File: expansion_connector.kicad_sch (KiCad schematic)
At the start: 18 parts, among them J18 ASP-218650-01_mounting_holes, J19 Plug_Samtec_UMPT-06-06.5-G-V-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

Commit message: [#83396] WIP: Route PCIe on expansion connector, change Expansion connector pinout to ease out routing PCIe
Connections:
- net DP1.AUX+: now also J18.B08; no longer J18.Y18
- net DP1.AUX-: now also J18.B09; no longer J18.Y19
- net DP1.TX0+: now also J18.B12; no longer J18.Y22
- net DP1.TX0-: now also J18.B13; no longer J18.Y23
- net DP1.TX1+: now also J18.B16; no longer J18.Y26
- net DP1.TX1-: now also J18.B17; no longer J18.Y27
- net DP1.TX2+: now also J18.B20; no longer J18.Y30
- net DP1.TX2-: now also J18.B21; no longer J18.Y31
- net DP1.TX3+: now also J18.B24; no longer J18.Y34
- net DP1.TX3-: now also J18.B25; no longer J18.Y35
- net PCIe_{C2x1}.CLK+: now also J18.Y38; no longer J18.B20
- net PCIe_{C2x1}.CLK-: now also J18.Y39; no longer J18.B21
- net PCIe_{C2x1}.RX0+: now also J18.Y35; no longer J18.B13
- net PCIe_{C2x1}.RX0-: now also J18.Y34; no longer J18.B12
- net PCIe_{C2x1}.~{CLKREQ}: now also J18.Z13; no longer J18.B17
- net PCIe_{C2x1}.~{RST}: now also J18.Z12; no longer J18.B16
- net PCIe_{C3x2}.CLK+: now also J18.Y27; no longer J18.Z21
- net PCIe_{C3x2}.CLK-: now also J18.Y26; no longer J18.Z20
- net PCIe_{C3x2}.RX0+: now also J18.Y19; no longer J18.Z17
- net PCIe_{C3x2}.RX0-: now also J18.Y18; no longer J18.Z16
- net PCIe_{C3x2}.RX1+: now also J18.Y23; no longer J18.Z13
- net PCIe_{C3x2}.RX1-: now also J18.Y22; no longer J18.Z12
- net PET0_C2_N: now also J18.Y31; no longer J18.B09
- net PET0_C2_P: now also J18.Y30; no longer J18.B08
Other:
- note removed: "----CSI----"
- note removed: "----PCIE----"
- note removed: "----RGMII----"
- note removed: "65 L K ... B A 64 . : 2 1"
- note removed: "AGX"
- note removed: "FMC"
- note removed: "M 40 39 38 ... 4 3 2 1 L K . : B A Z Y"
- note removed: "Perypherials"
- note removed: "We can change FMC pinout according to how hard it woud be to route it"
- note removed: "Z1 Y6 ... Y1"
- moved on the sheet: C213, C214

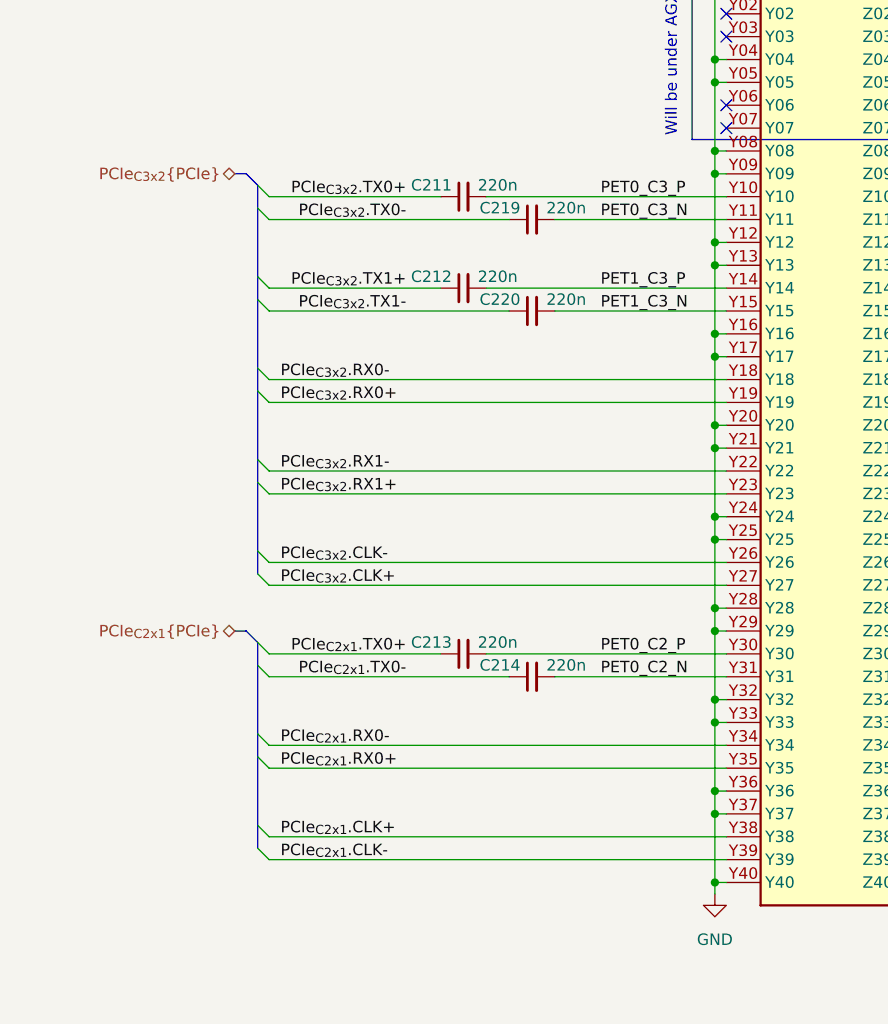
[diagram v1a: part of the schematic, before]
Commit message: [#83396] Route PCIe on expansion connector
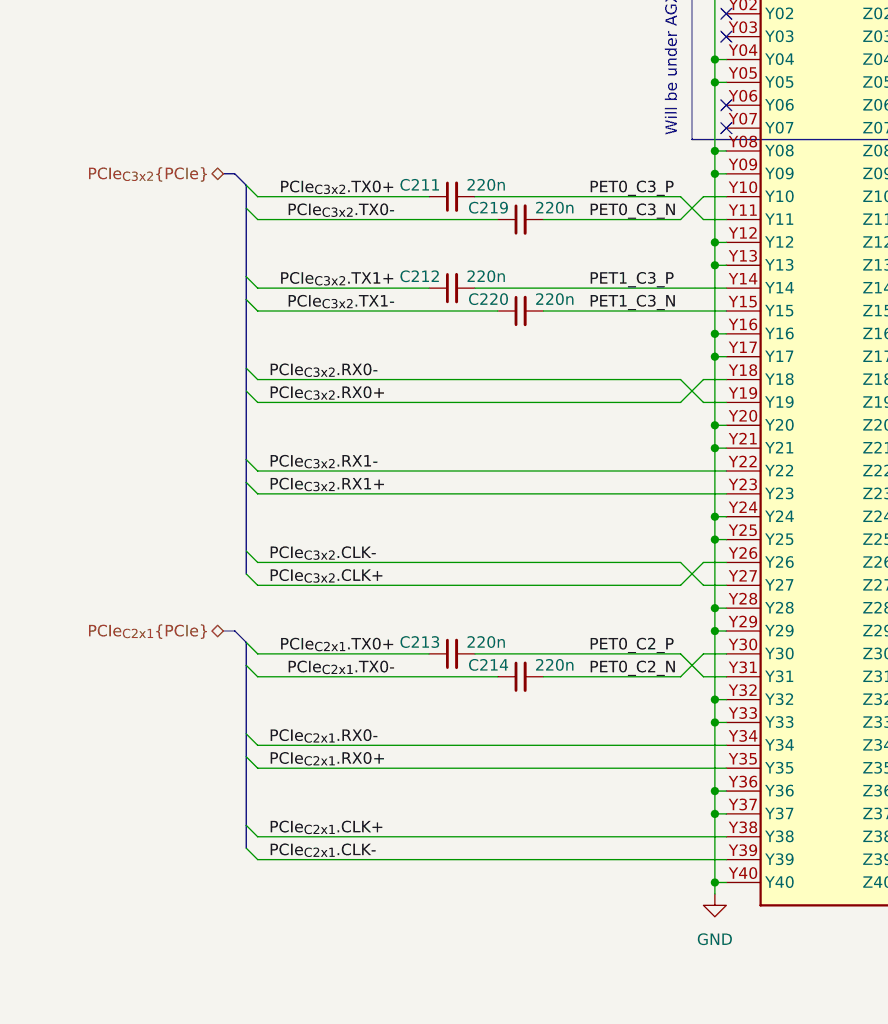
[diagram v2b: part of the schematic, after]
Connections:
- net PCIe_{C3x2}.CLK+: now also J18.Y26; no longer J18.Y27
- net PCIe_{C3x2}.CLK-: now also J18.Y27; no longer J18.Y26
- net PCIe_{C3x2}.RX0+: now also J18.Y18; no longer J18.Y19
- net PCIe_{C3x2}.RX0-: now also J18.Y19; no longer J18.Y18
- net PET0_C2_N: now also J18.Y30; no longer J18.Y31
- net PET0_C2_P: now also J18.Y31; no longer J18.Y30
- net PET0_C3_N: now also J18.Y10; no longer J18.Y11
- net PET0_C3_P: now also J18.Y11; no longer J18.Y10
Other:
- moved on the sheet: C211, C212, C213, C214, C219, C220

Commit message: [#83396] WIP: Route out DP
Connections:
- net DP1.AUX+: now also J18.A22; no longer J18.B08
- net DP1.AUX-: now also J18.A23; no longer J18.B09
- net DP1.TX0+: now also J18.A26; no longer J18.B12
- net DP1.TX0-: now also J18.A27; no longer J18.B13
- net DP1.TX1+: now also J18.A30; no longer J18.B16
- net DP1.TX1-: now also J18.A31; no longer J18.B17
- net DP1.TX2+: now also J18.A34; no longer J18.B20
- net DP1.TX2-: now also J18.A35; no longer J18.B21
- net DP1.TX3+: now also J18.A38; no longer J18.B24
- net DP1.TX3-: now also J18.A39; no longer J18.B25
- net DP3.AUX+: now also J18.B08; no longer J18.A22
- net DP3.AUX-: now also J18.B09; no longer J18.A23
- net DP3.TX0+: now also J18.B12; no longer J18.A26
- net DP3.TX0-: now also J18.B13; no longer J18.A27
- net DP3.TX1+: now also J18.B16; no longer J18.A30
- net DP3.TX1-: now also J18.B17; no longer J18.A31
- net DP3.TX2+: now also J18.B20; no longer J18.A34
- net DP3.TX2-: now also J18.B21; no longer J18.A35
- net DP3.TX3+: now also J18.B24; no longer J18.A38
- net DP3.TX3-: now also J18.B25; no longer J18.A39
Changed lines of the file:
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@@
 	)
 	(label "DP3.TX3-"
-		(at 74.93 260.35 0)
-		(effects
-			(font
-				(size 1.27 1.27)
-			)
-			(justify left bottom)
+		(at 125.73 224.79 180)
+		(effects
+			(font
+				(size 1.27 1.27)
+			)
+			(justify right bottom)
 		)
 	)
@@
 	)
 	(label "DP3.TX2+"
-		(at 74.93 247.65 0)
-		(effects
-			(font
-				(size 1.27 1.27)
-			)
-			(justify left bottom)
+		(at 125.73 212.09 180)
+		(effects
+			(font
+				(size 1.27 1.27)
+			)
+			(justify right bottom)
 		)
 	)
@@
 	)
 	(label "DP3.TX0+"
-		(at 74.93 227.33 0)
-		(effects
-			(font
-				(size 1.27 1.27)
-			)
-			(justify left bottom)
+		(at 125.73 191.77 180)
+		(effects
+			(font
+				(size 1.27 1.27)
+			)
+			(justify right bottom)
 		)
 	)
@@
 	)
 	(label "DP1.TX1+"
-		(at 125.73 201.93 180)
-		(effects
-			(font
-				(size 1.27 1.27)
-			)
-			(justify right bottom)
+		(at 74.93 237.49 0)
+		(effects
+			(font
+				(size 1.27 1.27)
+			)
+			(justify left bottom)
 		)
 	)
@@
 	)
 	(label "DP1.TX1-"
-		(at 125.73 204.47 180)
-		(effects
-			(font
-				(size 1.27 1.27)
-			)
-			(justify right bottom)
+		(at 74.93 240.03 0)
+		(effects
+			(font
+				(size 1.27 1.27)
+			)
+			(justify left bottom)
 		)
 	)
@@
 	)
 	(label "DP1.TX2+"
-		(at 125.73 212.09 180)
-		(effects
-			(font
-				(size 1.27 1.27)
-			)
-			(justify right bottom)
+		(at 74.93 247.65 0)
+		(effects
+			(font
+				(size 1.27 1.27)
+			)
+			(justify left bottom)
 		)
 	)
@@
 	)
 	(label "DP1.TX2-"
-		(at 125.73 214.63 180)
-		(effects
-			(font
-				(size 1.27 1.27)
-			)
-			(justify right bottom)
+		(at 74.93 250.19 0)
+		(effects
+			(font
+				(size 1.27 1.27)
+			)
+			(justify left bottom)
 		)
 	)
@@
 	)
 	(label "DP3.AUX+"
-		(at 74.93 217.17 0)
-		(effects
-			(font
-				(size 1.27 1.27)
-			)
-			(justify left bottom)
+		(at 125.73 181.61 180)
+		(effects
+			(font
+				(size 1.27 1.27)
+			)
+			(justify right bottom)
 		)
 	)
@@
 	)
 	(label "DP3.AUX-"
-		(at 74.93 219.71 0)
-		(effects
-			(font
-				(size 1.27 1.27)
-			)
-			(justify left bottom)
+		(at 125.73 184.15 180)
+		(effects
+			(font
+				(size 1.27 1.27)
+			)
+			(justify right bottom)
 		)
 	)
@@
 	)
 	(label "DP3.TX0-"
-		(at 74.93 229.87 0)
-		(effects
-			(font
-				(size 1.27 1.27)
-			)
-			(justify left bottom)
+		(at 125.73 194.31 180)
+		(effects
+			(font
+				(size 1.27 1.27)
+			)
+			(justify right bottom)
 		)
 	)
@@
 	)
 	(label "DP1.TX3-"
-		(at 125.73 224.79 180)
-		(effects
-			(font
-				(size 1.27 1.27)
-			)
-			(justify right bottom)
+		(at 74.93 260.35 0)
+		(effects
+			(font
+				(size 1.27 1.27)
+			)
+			(justify left bottom)
 		)
 	)
@@
 	)
 	(label "DP1.TX0-"
-		(at 125.73 194.31 180)
-		(effects
-			(font
-				(size 1.27 1.27)
-			)
-			(justify right bottom)
+		(at 74.93 229.87 0)
+		(effects
+			(font
+				(size 1.27 1.27)
+			)
+			(justify left bottom)
 		)
 	)
@@
 	)
 	(label "DP3.TX1-"
-		(at 74.93 240.03 0)
-		(effects
-			(font
-				(size 1.27 1.27)
-			)
-			(justify left bottom)
+		(at 125.73 204.47 180)
+		(effects
+			(font
+				(size 1.27 1.27)
+			)
+			(justify right bottom)
 		)
 	)
@@
 	)
 	(label "DP1.AUX+"
-		(at 125.73 181.61 180)
-		(effects
-			(font
-				(size 1.27 1.27)
-			)
-			(justify right bottom)
+		(at 74.93 217.17 0)
+		(effects
+			(font
+				(size 1.27 1.27)
+			)
+			(justify left bottom)
 		)
 	)
@@
 	)
 	(label "DP1.AUX-"
-		(at 125.73 184.15 180)
-		(effects
-			(font
-				(size 1.27 1.27)
-			)
-			(justify right bottom)
+		(at 74.93 219.71 0)
+		(effects
+			(font
+				(size 1.27 1.27)
+			)
+			(justify left bottom)
 		)
 	)
@@
 	)
 	(label "DP1.TX3+"
-		(at 125.73 222.25 180)
-		(effects
-			(font
-				(size 1.27 1.27)
-			)
-			(justify right bottom)
+		(at 74.93 257.81 0)
+		(effects
+			(font
+				(size 1.27 1.27)
+			)
+			(justify left bottom)
 		)
 	)
@@
 	)
 	(label "DP1.TX0+"
-		(at 125.73 191.77 180)
-		(effects
-			(font
-				(size 1.27 1.27)
-			)
-			(justify right bottom)
+		(at 74.93 227.33 0)
+		(effects
+			(font
+				(size 1.27 1.27)
+			)
+			(justify left bottom)
 		)
 	)
@@
 	)
 	(label "DP3.TX2-"
-		(at 74.93 250.19 0)
-		(effects
-			(font
-				(size 1.27 1.27)
-			)
-			(justify left bottom)
+		(at 125.73 214.63 180)
+		(effects
+			(font
+				(size 1.27 1.27)
+			)
+			(justify right bottom)
 		)
 	)
@@
 	)
 	(label "DP3.TX3+"
-		(at 74.93 257.81 0)
-		(effects
-			(font
-				(size 1.27 1.27)
-			)
-			(justify left bottom)
+		(at 125.73 222.25 180)
+		(effects
+			(font
+				(size 1.27 1.27)
+			)
+			(justify right bottom)
 		)
 	)
 	(label "DP3.TX1+"
-		(at 74.93 237.49 0)
-		(effects
-			(font
-				(size 1.27 1.27)
-			)
-			(justify left bottom)
+		(at 125.73 201.93 180)
+		(effects
+			(font
+				(size 1.27 1.27)
+			)
+			(justify right bottom)
 		)
 	)
@@
 		)
 	)
-	(hierarchical_label "DP1{DP}"
+	(hierarchical_label "DP3{DP}"
 		(shape input)
 		(at 130.81 179.07 0)
@@
 		)
 	)
-	(hierarchical_label "DP3{DP}"
+	(hierarchical_label "DP1{DP}"
 		(shape input)
 		(at 68.58 214.63 180)

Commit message: [#83396] WIP: Route out DP
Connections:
- net DP1.AUX+: now also J18.A23; no longer J18.A22
- net DP1.AUX-: now also J18.A22; no longer J18.A23
- net DP1.TX0+: now also J18.A27; no longer J18.A26
- net DP1.TX0-: now also J18.A26; no longer J18.A27
- net DP1.TX1+: now also J18.A31; no longer J18.A30
- net DP1.TX1-: now also J18.A30; no longer J18.A31
- net DP1.TX2+: now also J18.A35; no longer J18.A34
- net DP1.TX2-: now also J18.A34; no longer J18.A35
- net DP1.TX3+: now also J18.A39; no longer J18.A38
- net DP1.TX3-: now also J18.A38; no longer J18.A39
- net DP2.AUX+: now also J18.A03; no longer J18.A02
- net DP2.AUX-: now also J18.A02; no longer J18.A03
- net DP2.TX0+: now also J18.A07; no longer J18.A06
- net DP2.TX0-: now also J18.A06; no longer J18.A07
- net DP2.TX1+: now also J18.A11; no longer J18.A10
- net DP2.TX1-: now also J18.A10; no longer J18.A11
- net DP2.TX2+: now also J18.A15; no longer J18.A14
- net DP2.TX2-: now also J18.A14; no longer J18.A15
- net DP2.TX3+: now also J18.A19; no longer J18.A18
- net DP2.TX3-: now also J18.A18; no longer J18.A19
- net DP3.AUX+: now also J18.B25; no longer J18.B08
- net DP3.AUX-: now also J18.B24; no longer J18.B09
- net DP3.TX0+: now also J18.B21; no longer J18.B12
- net DP3.TX0-: now also J18.B20; no longer J18.B13
- net DP3.TX1+: now also J18.B17; no longer J18.B16
- net DP3.TX1-: now also J18.B16; no longer J18.B17
- net DP3.TX2+: now also J18.B12; no longer J18.B20
- net DP3.TX2-: now also J18.B13; no longer J18.B21
- net DP3.TX3+: now also J18.B08; no longer J18.B24
- net DP3.TX3-: now also J18.B09; no longer J18.B25

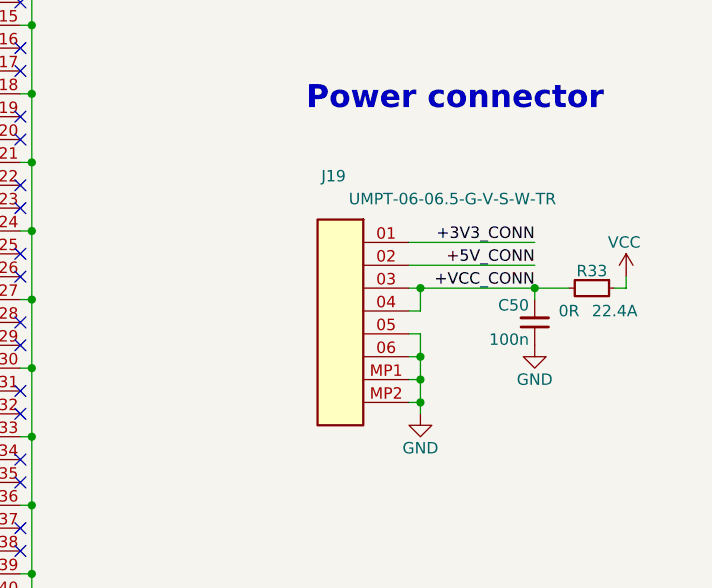
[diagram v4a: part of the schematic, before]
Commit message: [#83396] Update all symbols from library and clear all ERC errors
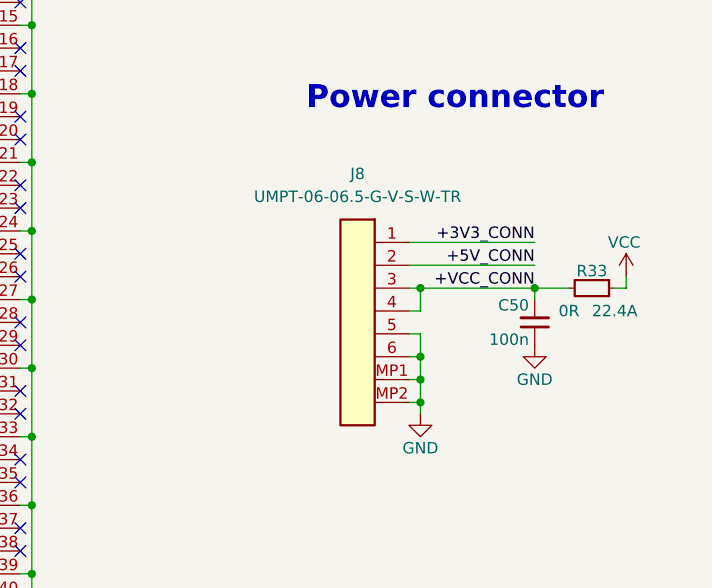
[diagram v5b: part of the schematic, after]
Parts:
- removed J19: Plug_Samtec_UMPT-06-06.5-G-V-S-TR, antmicro-footprints:Plug_Samtec_UMPT-06-06.5-G-V-S-TR, symbol antmicroB2BConnectors:Plug_Samtec_UMPT-06-06.5-G-V-S-TR
- added J8: Plug_Samtec_UMPT_1x6_UMPT-06-06.5-G-V-S-TR, antmicro-footprints:Conn_Plug_Samtec_UMPT_1x6_UMPT-06-06.5-G-V-S-TR, symbol antmicroB2BConnectors:Plug_Samtec_UMPT_1x6_UMPT-06-06.5-G-V-S-TR
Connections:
- net +3V3_CONN: now also J8.1
- net +5V_CONN: now also J8.2
- net +VCC_CONN: now also J8.3, J8.4
- net GND: now also J8.5, J8.6, J8.MP1, J8.MP2
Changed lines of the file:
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@@
 	)
 	(symbol
-		(lib_id "antmicroB2BConnectors:Plug_Samtec_UMPT-06-06.5-G-V-S-TR")
-		(at 337.82 223.52 0)
-		(mirror y)
-		(unit 1)
-		(exclude_from_sim no)
-		(in_bom yes)
-		(on_board yes)
-		(dnp no)
-		(property "Reference" "J19"
-			(at 329.438 216.154 0)
-			(effects
-				(font
-					(size 1.27 1.27)
-					(thickness 0.15)
-				)
-			)
-		)
-		(property "Value" "Plug_Samtec_UMPT-06-06.5-G-V-S-TR"
-			(at 313.69 231.14 0)
-			(effects
-				(font
-					(size 1.27 1.27)
-					(thickness 0.15)
-				)
-				(justify left bottom)
-				(hide yes)
-			)
-		)
-		(property "Footprint" "antmicro-footprints:Plug_Samtec_UMPT-06-06.5-G-V-S-TR"
-			(at 313.69 233.68 0)
-			(effects
-				(font
-					(size 1.27 1.27)
-					(thickness 0.15)
-				)
-				(justify left bottom)
-				(hide yes)
-			)
-		)
-		(property "Datasheet" "https://suddendocs.samtec.com/catalog_english/umpt.pdf"
-			(at 313.69 236.22 0)
-			(effects
-				(font
-					(size 1.27 1.27)
-					(thickness 0.15)
-				)
-				(justify left bottom)
-				(hide yes)
-			)
-		)
-		(property "Description" "2.00 mm mPOWER® Ultra Micro Power Terminal, Vertical"
-			(at 313.69 238.76 0)
-			(effects
-				(font
-					(size 1.27 1.27)
-					(thickness 0.15)
-				)
-				(justify left bottom)
-				(hide yes)
-			)
-		)
-		(property "MPN" "UMPT-06-06.5-G-V-S-W-TR"
-			(at 342.646 218.694 0)
-			(effects
-				(font
-					(size 1.27 1.27)
-					(thickness 0.15)
-				)
-			)
-		)
-		(property "Manufacturer" "Samtec"
-			(at 313.69 241.3 0)
-			(effects
-				(font
-					(size 1.27 1.27)
-					(thickness 0.15)
-				)
-				(justify left bottom)
-				(hide yes)
-			)
-		)
-		(property "Author" "Antmicro"
-			(at 313.69 243.84 0)
-			(effects
-				(font
-					(size 1.27 1.27)
-					(thickness 0.15)
-				)
-				(justify left bottom)
-				(hide yes)
-			)
-		)
-		(property "License" "Apache-2.0"
-			(at 313.69 246.38 0)
-			(effects
-				(font
-					(size 1.27 1.27)
-					(thickness 0.15)
-				)
-				(justify left bottom)
-				(hide yes)
-			)
-		)
-		(pin "04"
-		)
-		(pin "02"
-		)
-		(pin "03"
-		)
-		(pin "01"
-		)
-		(pin "MP2"
-		)
-		(pin "05"
-		)
-		(pin "MP1"
-		)
-		(pin "06"
-		)
-		(instances
-			(project ""
-				(path "/f569b0be-0afd-48b7-93ee-28582a4c645c/5fb038ee-4d59-43de-81a4-b4c993aa7149"
-					(reference "J19")
-					(unit 1)
-				)
-			)
-		)
-	)
-	(symbol
 		(lib_id "antmicropower:GND")
 		(at 351.79 234.95 0)
@@
 				)
 			)
+		)
+	)
+	(symbol
+		(lib_id "antmicroB2BConnectors:Plug_Samtec_UMPT_1x6_UMPT-06-06.5-G-V-S-TR")
+		(at 337.82 223.52 0)
+		(mirror y)
+		(unit 1)
+		(exclude_from_sim no)
+		(in_bom yes)
+		(on_board yes)
+		(dnp no)
+		(fields_autoplaced yes)
+		(property "Reference" "J8"
+			(at 332.105 215.9 0)
+			(effects
+				(font
+					(size 1.27 1.27)
+					(thickness 0.15)
+				)
+			)
+		)
+		(property "Value" "Plug_Samtec_UMPT_1x6_UMPT-06-06.5-G-V-S-TR"
+			(at 314.96 231.14 0)
+			(effects
+				(font
+					(size 1.27 1.27)
+					(thickness 0.15)
+				)
+				(justify left bottom)
+				(hide yes)
+			)
+		)
+		(property "Footprint" "antmicro-footprints:Conn_Plug_Samtec_UMPT_1x6_UMPT-06-06.5-G-V-S-TR"
+			(at 314.96 233.68 0)
+			(effects
+				(font
+					(size 1.27 1.27)
+					(thickness 0.15)
+				)
+				(justify left bottom)
+				(hide yes)
+			)
+		)
+		(property "Datasheet" "https://suddendocs.samtec.com/catalog_english/umpt.pdf"
+			(at 314.96 236.22 0)
+			(effects
+				(font
+					(size 1.27 1.27)
+					(thickness 0.15)
+				)
+				(justify left bottom)
+				(hide yes)
+			)
+		)
+		(property "Description" "2.00 mm mPOWER® Ultra Micro Power Terminal, Vertical"
+			(at 314.96 248.92 0)
+			(effects
+				(font
+					(size 1.27 1.27)
+					(thickness 0.15)
+				)
+				(justify left bottom)
+				(hide yes)
+			)
+		)
+		(property "MPN" "UMPT-06-06.5-G-V-S-W-TR"
+			(at 332.105 218.44 0)
+			(effects
+				(font
+					(size 1.27 1.27)
+					(thickness 0.15)
+				)
+			)
+		)
+		(property "Manufacturer" "Samtec"
+			(at 314.96 241.3 0)
+			(effects
+				(font
+					(size 1.27 1.27)
+					(thickness 0.15)
+				)
+				(justify left bottom)
+				(hide yes)
+			)
+		)
+		(property "Author" "Antmicro"
+			(at 314.96 243.84 0)
+			(effects
+				(font
+					(size 1.27 1.27)
+					(thickness 0.15)
+				)
+				(justify left bottom)
+				(hide yes)
+			)
+		)
+		(property "License" "Apache-2.0"
+			(at 314.96 246.38 0)
+			(effects
+				(font
+					(size 1.27 1.27)
+					(thickness 0.15)
+				)
+				(justify left bottom)
+				(hide yes)
+			)
+		)
+		(pin "1"
+		)
+		(pin "MP2"
+		)
+		(pin "MP1"
+		)
+		(pin "5"
+		)
+		(pin "6"
+		)
+		(pin "3"
+		)
+		(pin "4"
+		)
+		(pin "2"
+		)
+		(instances
+			(project ""
+				(path "/f569b0be-0afd-48b7-93ee-28582a4c645c/5fb038ee-4d59-43de-81a4-b4c993aa7149"
+					(reference "J8")
+					(unit 1)
+				)
+			)
